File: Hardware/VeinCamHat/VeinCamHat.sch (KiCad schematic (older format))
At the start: 65 parts, among them J1 USB_B_Micro, J2 Raspberry_Pi_2_3, Q1 BSD235N, Q2 MMUN2133L, SW1 SW_SPST, U1 MCP3021, U2 TPS61092, U3 MCP73871

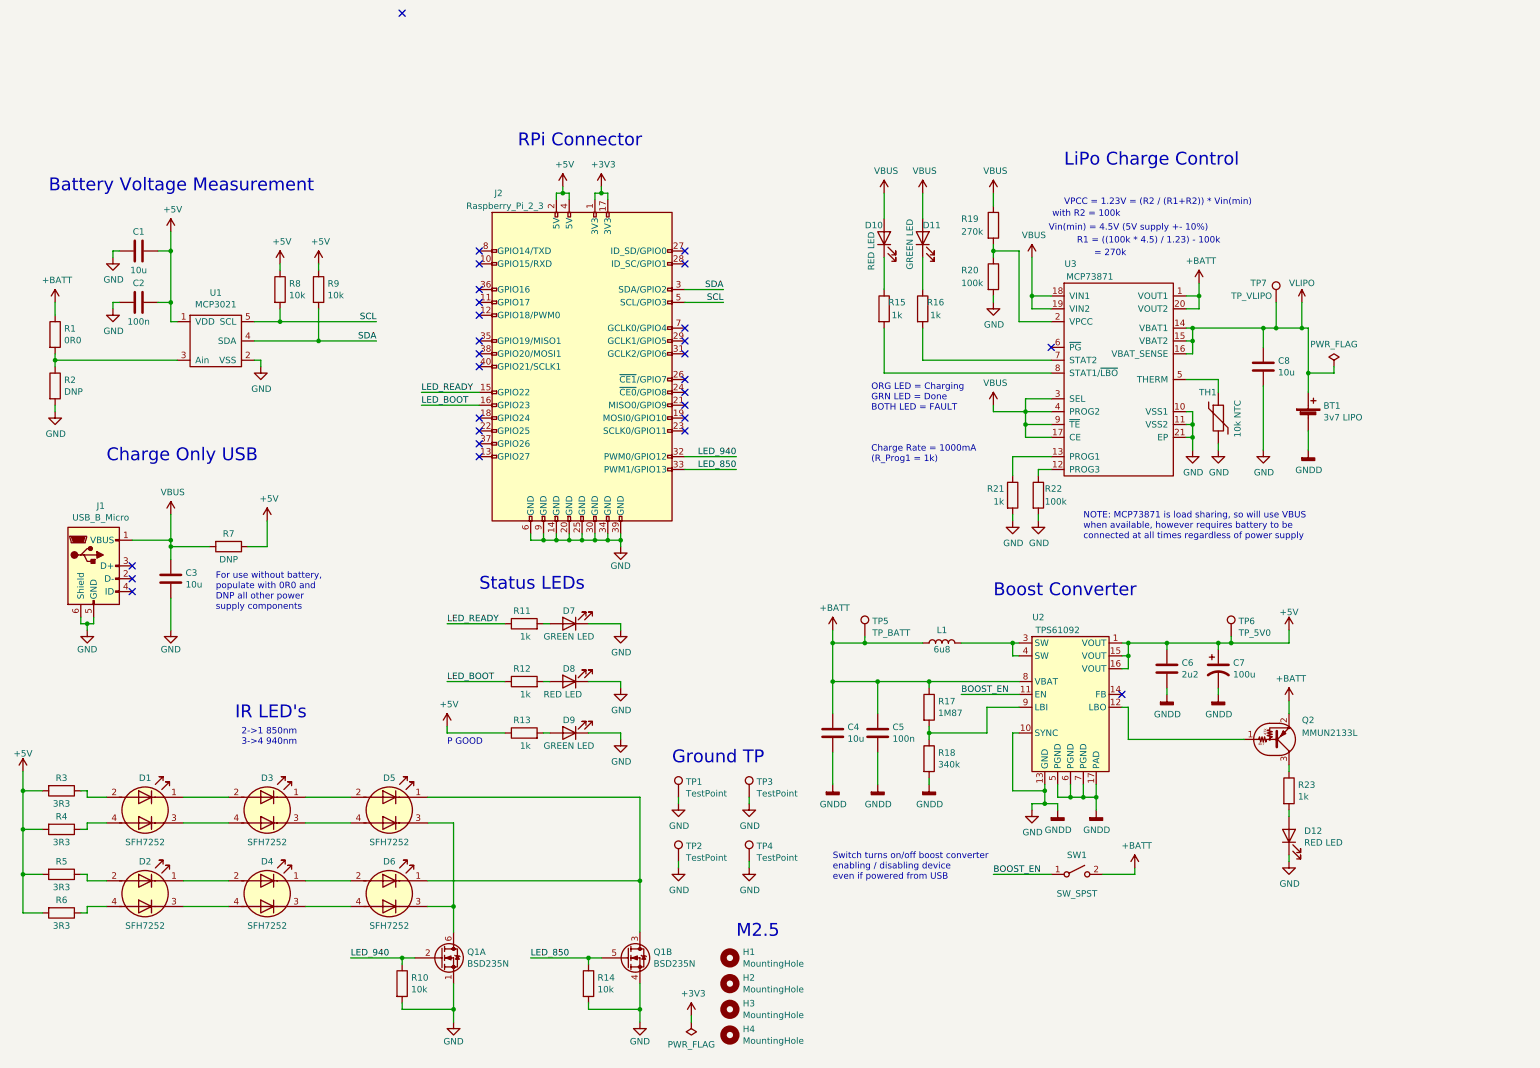
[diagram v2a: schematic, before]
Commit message: Added footprints for VeinCamHat and begun layout
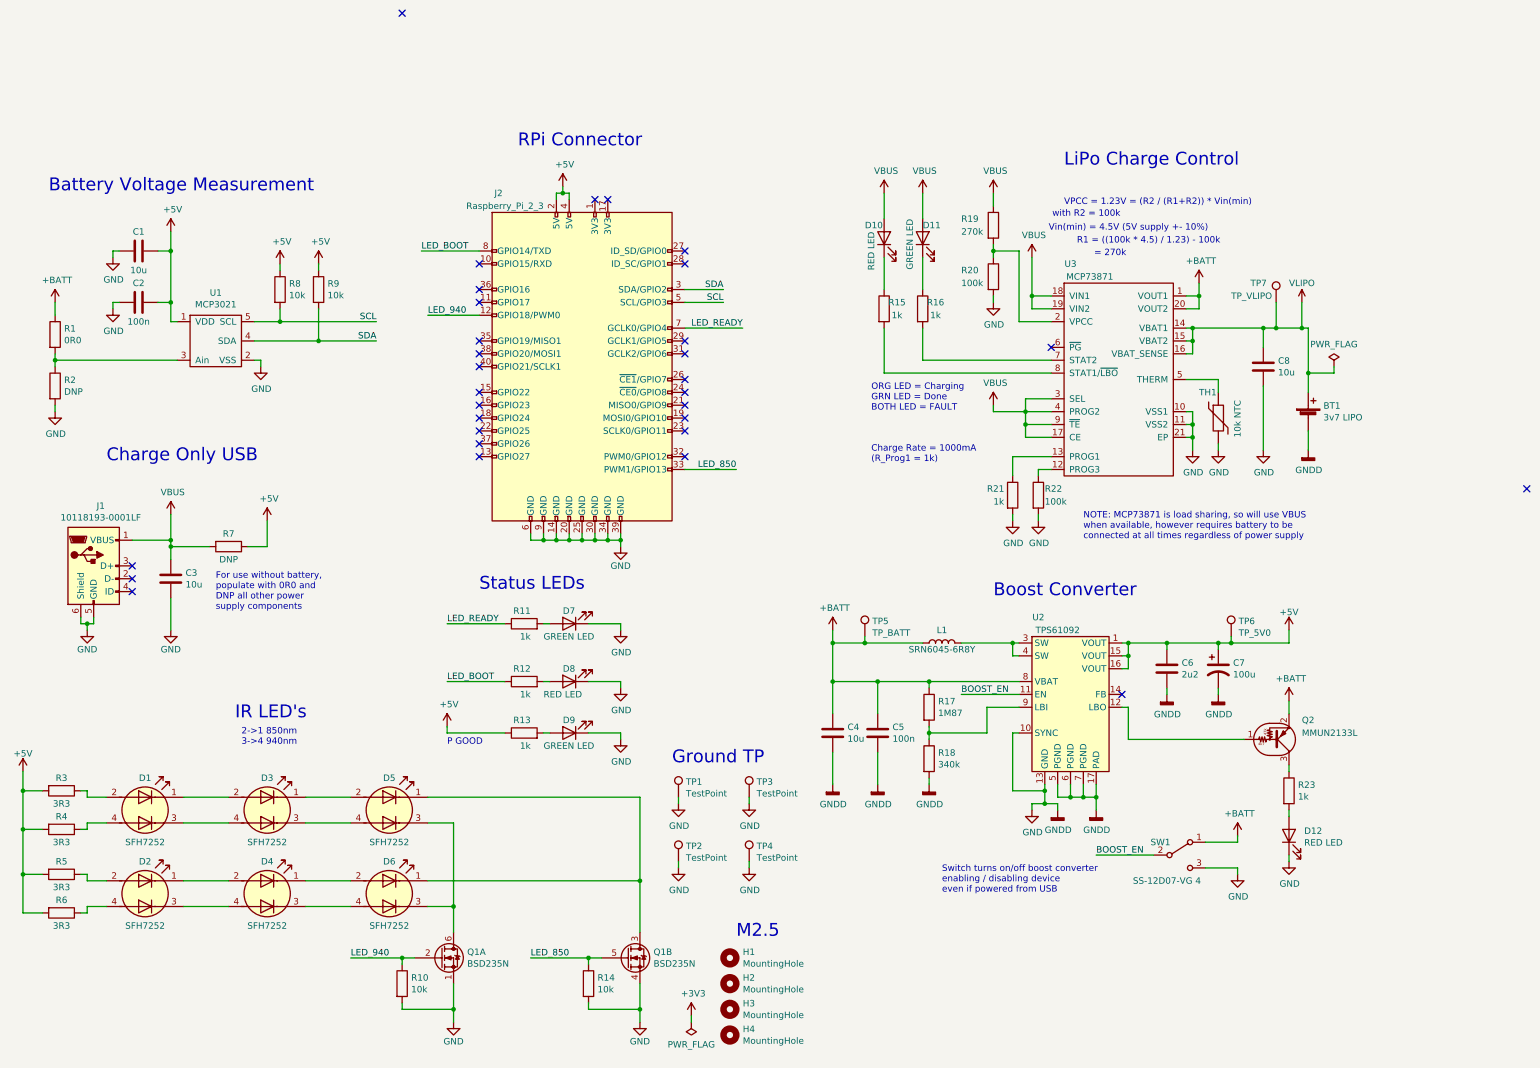
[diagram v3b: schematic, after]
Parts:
- removed SW1: SW_SPST, symbol Switch:SW_SPST
- added SW1: SS-12D07-VG 4, VeinCam_Footprints:SS-12D07-VG4, symbol Switch:SW_SPDT
- D1, D2, D3, D4, D5, D6: footprint (none) -> VeinCam_Footprints:SFH7252
- J1: value USB_B_Micro -> 10118193-0001LF; footprint (none) -> VeinCam_Footprints:10118193-0001LF
- J2: footprint (none) -> Connector_PinSocket_2.54mm:PinSocket_2x20_P2.54mm_Vertical
- L1: value 6u8 -> SRN6045-6R8Y; footprint (none) -> VeinCam_Footprints:SRN6045
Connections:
- net +3V3: no longer J2.1 (3V3), J2.17 (3V3)
- net +BATT: now also SW1.1 (A)
- net BOOST_EN: now also SW1.2 (B)
- net GND: now also SW1.3 (C)
- net LED_940: now also J2.12 (GPIO18/PWM0); no longer J2.32 (PWM0/GPIO12)
- net LED_BOOT: now also J2.8 (GPIO14/TXD); no longer J2.16 (GPIO23)
- net LED_READY: now also J2.7 (GCLK0/GPIO4); no longer J2.15 (GPIO22)
- no-connect marks 28 -> 31
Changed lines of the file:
@@
 P 1250 3900
 F 0 "J1" H 1305 4367 50  0000 C CNN
-F 1 "USB_B_Micro" H 1305 4276 50  0000 C CNN
-F 2 "" H 1400 3850 50  0001 C CNN
+F 1 "10118193-0001LF" H 1305 4276 50  0000 C CNN
+F 2 "VeinCam_Footprints:10118193-0001LF" H 1400 3850 50  0001 C CNN
 F 3 "~" H 1400 3850 50  0001 C CNN
 	1    1250 3900
@@
 P 7850 4500
 F 0 "L1" V 7950 4500 50  0000 C CNN
-F 1 "6u8" V 7800 4500 50  0000 C CNN
-F 2 "" H 7850 4500 50  0001 C CNN
+F 1 "SRN6045-6R8Y" V 7800 4500 50  0000 C CNN
+F 2 "VeinCam_Footprints:SRN6045" H 7850 4500 50  0001 C CNN
 F 3 "~" H 7850 4500 50  0001 C CNN
 	1    7850 4500
@@
 Wire Wire Line
 	7350 4800 7750 4800
-Text Label 8250 6300 0    50   ~ 0
+Text Label 9050 6150 0    50   ~ 0
 BOOST_EN
 Wire Wire Line
-	8250 6300 8700 6300
-$Comp
-L Switch:SW_SPST SW1
-U 1 1 5CF1111C
-P 8900 6300
-F 0 "SW1" H 8900 6450 50  0000 C CNN
-F 1 "SW_SPST" H 8900 6150 50  0000 C CNN
-F 2 "" H 8900 6300 50  0001 C CNN
-F 3 "" H 8900 6300 50  0001 C CNN
-	1    8900 6300
-	1    0    0    -1
-$EndComp
-Wire Wire Line
-	9100 6300 9350 6300
-Wire Wire Line
-	9350 6300 9350 6250
+	9050 6150 9500 6150
+Wire Wire Line
+	9900 6050 10150 6050
+Wire Wire Line
+	10150 6050 10150 6000
 $Comp
 L power:+BATT #PWR0130
 U 1 1 5CF1F81A
-P 9350 6250
-F 0 "#PWR0130" H 9350 6100 50  0001 C CNN
-F 1 "+BATT" H 9365 6423 50  0000 C CNN
-F 2 "" H 9350 6250 50  0001 C CNN
-F 3 "" H 9350 6250 50  0001 C CNN
-	1    9350 6250
-	1    0    0    -1
-$EndComp
-Text Notes 7000 6350 0    50   ~ 0
+P 10150 6000
+F 0 "#PWR0130" H 10150 5850 50  0001 C CNN
+F 1 "+BATT" H 10165 6173 50  0000 C CNN
+F 2 "" H 10150 6000 50  0001 C CNN
+F 3 "" H 10150 6000 50  0001 C CNN
+	1    10150 6000
+	1    0    0    -1
+$EndComp
+Text Notes 7850 6450 0    50   ~ 0
 Switch turns on/off boost converter\nenabling / disabling device\neven if powered from USB
 Text Notes 8950 3700 0    50   ~ 0
@@
 F 0 "J2" H 4400 3700 50  0000 C CNN
 F 1 "Raspberry_Pi_2_3" H 4450 3600 50  0000 C CNN
-F 2 "" H 5050 2350 50  0001 C CNN
+F 2 "Connector_PinSocket_2.54mm:PinSocket_2x20_P2.54mm_Vertical" H 5050 2350 50  0001 C CNN
 F 3 "https://www.raspberrypi.org/documentation/hardware/raspberrypi/schematics/rpi_SCH_3bplus_1p0_reduced.pdf" H 5050 2350 50  0001 C CNN
 	1    5050 2350
@@
 	1    0    0    -1
 $EndComp
-$Comp
-L power:+3V3 #PWR0137
-U 1 1 5D44522B
-P 5200 950
-F 0 "#PWR0137" H 5200 800 50  0001 C CNN
-F 1 "+3V3" H 5215 1123 50  0000 C CNN
-F 2 "" H 5200 950 50  0001 C CNN
-F 3 "" H 5200 950 50  0001 C CNN
-	1    5200 950
-	1    0    0    -1
-$EndComp
 NoConn ~ 5850 1450
 NoConn ~ 5850 1550
 Wire Wire Line
-	5850 3050 6250 3050
+	4250 1950 3850 1950
 Wire Wire Line
 	5850 3150 6250 3150
-Text Label 6250 3050 2    50   ~ 0
+Text Label 3850 1950 0    50   ~ 0
 LED_940
 Text Label 6250 3150 2    50   ~ 0
@@
 	5500 6350 5500 6750
 Connection ~ 5500 6350
-Text Label 3800 2550 0    50   ~ 0
+Text Label 6300 2050 2    50   ~ 0
 LED_READY
 Wire Wire Line
-	3800 2550 4250 2550
-Wire Wire Line
-	3800 2650 4250 2650
-Text Label 3800 2650 0    50   ~ 0
+	6300 2050 5850 2050
+Wire Wire Line
+	3800 1450 4250 1450
+Text Label 3800 1450 0    50   ~ 0
 LED_BOOT
 Text Label 4000 4350 0    50   ~ 0
@@
 F 0 "D1" H 1650 6050 50  0000 C CNN
 F 1 "SFH7252" H 1650 5550 50  0000 C CNN
-F 2 "" H 1680 5800 50  0001 C CNN
+F 2 "VeinCam_Footprints:SFH7252" H 1680 5800 50  0001 C CNN
 F 3 "~" H 1680 5800 50  0001 C CNN
 	1    1650 5800
@@
 F 0 "D2" H 1650 6700 50  0000 C CNN
 F 1 "SFH7252" H 1650 6200 50  0000 C CNN
-F 2 "" H 1680 6450 50  0001 C CNN
+F 2 "VeinCam_Footprints:SFH7252" H 1680 6450 50  0001 C CNN
 F 3 "~" H 1680 6450 50  0001 C CNN
 	1    1650 6450
@@
 F 0 "D4" H 2600 6700 50  0000 C CNN
 F 1 "SFH7252" H 2600 6200 50  0000 C CNN
-F 2 "" H 2630 6450 50  0001 C CNN
+F 2 "VeinCam_Footprints:SFH7252" H 2630 6450 50  0001 C CNN
 F 3 "~" H 2630 6450 50  0001 C CNN
 	1    2600 6450
@@
 F 0 "D6" H 3550 6700 50  0000 C CNN
 F 1 "SFH7252" H 3550 6200 50  0000 C CNN
-F 2 "" H 3580 6450 50  0001 C CNN
+F 2 "VeinCam_Footprints:SFH7252" H 3580 6450 50  0001 C CNN
 F 3 "~" H 3580 6450 50  0001 C CNN
 	1    3550 6450
@@
 F 0 "D5" H 3550 6050 50  0000 C CNN
 F 1 "SFH7252" H 3550 5550 50  0000 C CNN
-F 2 "" H 3580 5800 50  0001 C CNN
+F 2 "VeinCam_Footprints:SFH7252" H 3580 5800 50  0001 C CNN
 F 3 "~" H 3580 5800 50  0001 C CNN
 	1    3550 5800
@@
 F 0 "D3" H 2600 6050 50  0000 C CNN
 F 1 "SFH7252" H 2600 5550 50  0000 C CNN
-F 2 "" H 2630 5800 50  0001 C CNN
+F 2 "VeinCam_Footprints:SFH7252" H 2630 5800 50  0001 C CNN
 F 3 "~" H 2630 5800 50  0001 C CNN
 	1    2600 5800
@@
 	1    0    0    -1
 $EndComp
-NoConn ~ 4250 1450
 NoConn ~ 4250 1550
 NoConn ~ 4250 1750
 NoConn ~ 4250 1850
-NoConn ~ 4250 1950
 NoConn ~ 4250 2150
 NoConn ~ 4250 2250
@@
 NoConn ~ 5850 2250
 NoConn ~ 5850 2150
-NoConn ~ 5850 2050
-Wire Wire Line
-	5150 1050 5150 1000
-Wire Wire Line
-	5150 1000 5200 1000
-Wire Wire Line
-	5250 1000 5250 1050
-Wire Wire Line
-	5200 1000 5200 950
-Connection ~ 5200 1000
-Wire Wire Line
-	5200 1000 5250 1000
 $Comp
 L power:PWR_FLAG #FLG0101
@@
 	1    0    0    -1
 $EndComp
+$Comp
+L Switch:SW_SPDT SW1
+U 1 1 5C908079
+P 9700 6150
+F 0 "SW1" H 9550 6250 50  0000 C CNN
+F 1 "SS-12D07-VG 4" H 9600 5950 50  0000 C CNN
+F 2 "VeinCam_Footprints:SS-12D07-VG4" H 9700 6150 50  0001 C CNN
+F 3 "" H 9700 6150 50  0001 C CNN
+	1    9700 6150
+	1    0    0    -1
+$EndComp
+Wire Wire Line
+	9900 6250 10150 6250
+Wire Wire Line
+	10150 6250 10150 6300
+$Comp
+L power:GND #PWR0137
+U 1 1 5C942C6D
+P 10150 6300
+F 0 "#PWR0137" H 10150 6050 50  0001 C CNN
+F 1 "GND" H 10155 6127 50  0000 C CNN
+F 2 "" H 10150 6300 50  0001 C CNN
+F 3 "" H 10150 6300 50  0001 C CNN
+	1    10150 6300
+	1    0    0    -1
+$EndComp
+NoConn ~ 4250 2650
+NoConn ~ 5850 3050
+NoConn ~ 5150 1050
+NoConn ~ 5250 1050
+NoConn ~ 12400 3300
+NoConn ~ 4250 2550
 $EndSCHEMATC

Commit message: Changed plans for VeinCam Plus, both boards laid out
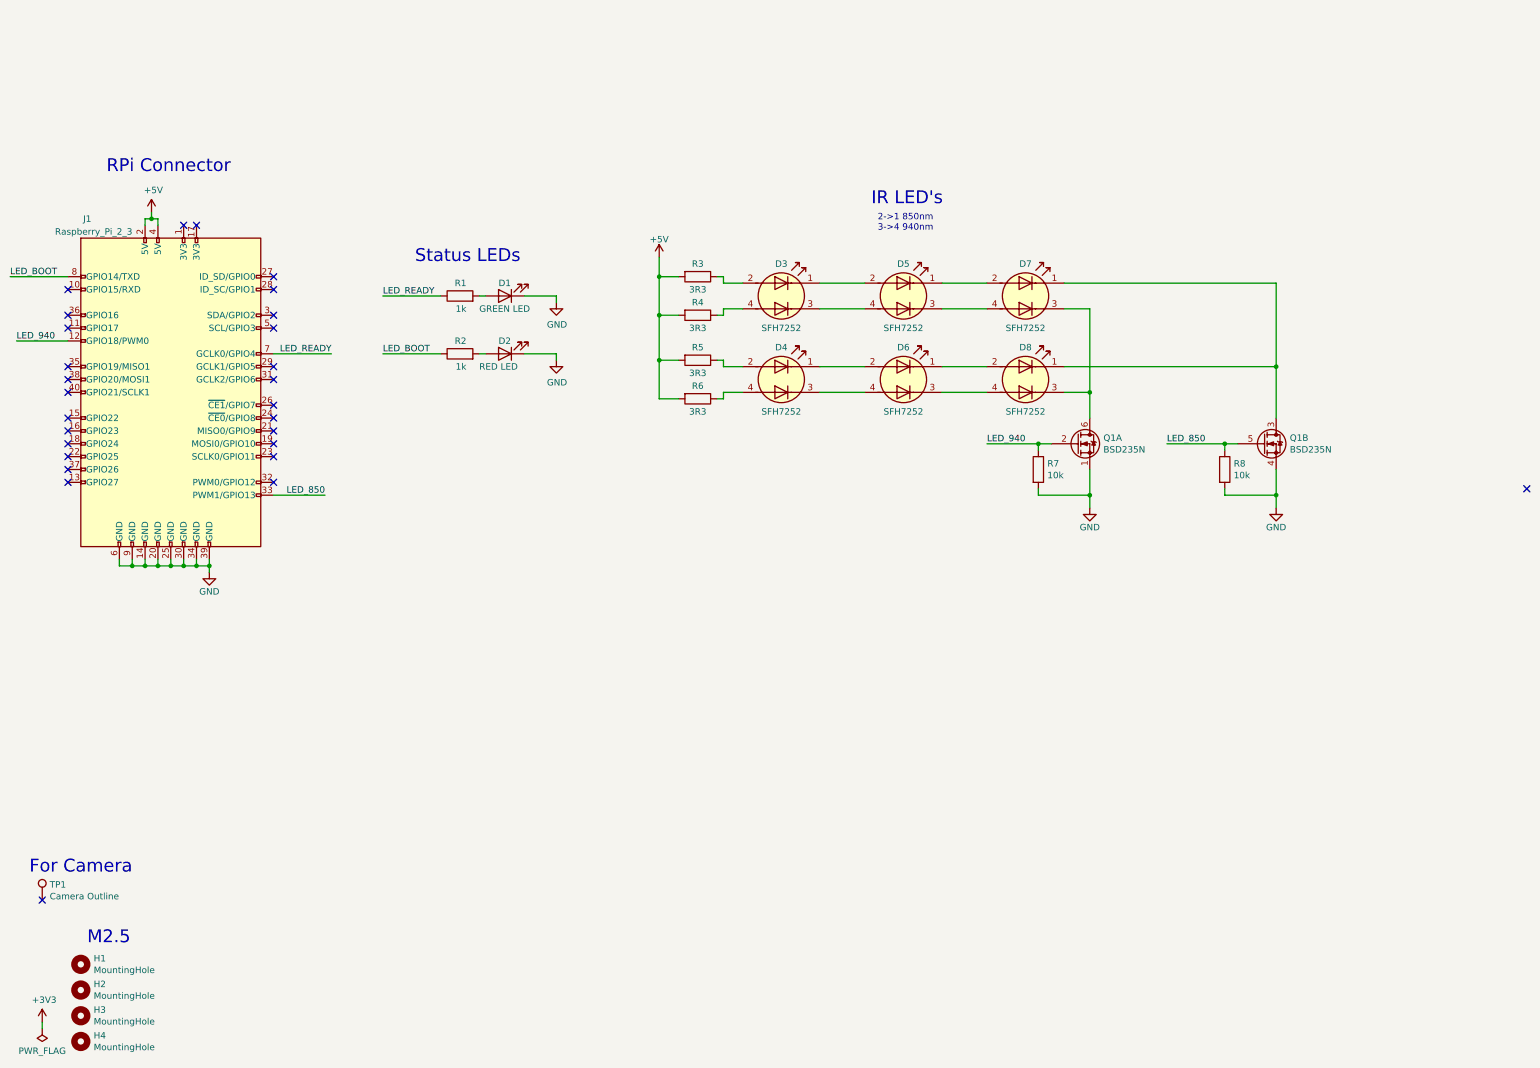
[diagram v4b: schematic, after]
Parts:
- removed BT1: 3v7 LIPO, Connector_JST:JST_XH_S02B-XH-A_1x02_P2.50mm_Horizontal, symbol Device:Battery_Cell
- removed C1, C3, C4, C8: 10u, Capacitor_SMD:C_0603_1608Metric, symbol Device:C
- removed C2, C5: 100n, Capacitor_SMD:C_0603_1608Metric, symbol Device:C
- removed C6: 2u2, Capacitor_SMD:C_0603_1608Metric, symbol Device:C
- removed C7: 100u, Capacitor_Tantalum_SMD:CP_EIA-7343-31_Kemet-D, symbol Device:CP1
- removed D10, D12: RED LED, LED_SMD:LED_0805_2012Metric, symbol Device:LED
- removed D11, D9: GREEN LED, LED_SMD:LED_0805_2012Metric, symbol Device:LED
- removed J1: 10118193-0001LF, VeinCam_Footprints:10118193-0001LF, symbol Connector:USB_B_Micro
- removed L1: SRN6045-6R8Y, VeinCam_Footprints:SRN6045, symbol Device:L
- removed Q2: MMUN2133L, Package_TO_SOT_SMD:SOT-23, symbol Transistor_BJT:DTA143Z
- removed R1: 0R0, Resistor_SMD:R_0603_1608Metric, symbol Device:R
- removed R13, R15, R16, R21, R23: 1k, Resistor_SMD:R_0603_1608Metric, symbol Device:R
- removed R17: 1M87, Resistor_SMD:R_0603_1608Metric, symbol Device:R
- removed R18: 340k, Resistor_SMD:R_0603_1608Metric, symbol Device:R
- removed R19: 270k, Resistor_SMD:R_0603_1608Metric, symbol Device:R
- removed R2: DNP, Resistor_SMD:R_0603_1608Metric, symbol Device:R
- removed R20, R22: 100k, Resistor_SMD:R_0603_1608Metric, symbol Device:R
- removed R7: DNP, Resistor_SMD:R_1206_3216Metric, symbol Device:R
- removed R8, R9: 10k, Resistor_SMD:R_0603_1608Metric, symbol Device:R
- removed SW1: SS-12D07-VG 4, VeinCam_Footprints:SS-12D07-VG4, symbol Switch:SW_SPDT
- removed TH1: 10k NTC, Resistor_SMD:R_0603_1608Metric, symbol Device:Thermistor
- removed TP2, TP3, TP4: TestPoint, TestPoint:TestPoint_THTPad_D1.0mm_Drill0.5mm, symbol Connector:TestPoint
- removed TP5: TP_BATT, TestPoint:TestPoint_Pad_D1.0mm, symbol Connector:TestPoint
- removed TP6: TP_5V0, TestPoint:TestPoint_Pad_D1.0mm, symbol Connector:TestPoint
- removed TP7: TP_VLIPO, TestPoint:TestPoint_Pad_D1.0mm, symbol Connector:TestPoint
- removed U1: MCP3021, Package_TO_SOT_SMD:SOT-23-5, symbol VeinCam_Symbols:MCP3021
- removed U2: TPS61092, Package_DFN_QFN:QFN-16-1EP_4x4mm_P0.65mm_EP2.5x2.5mm, symbol Regulator_Switching:TPS61092
- removed U3: MCP73871, Package_DFN_QFN:QFN-20-1EP_4x4mm_P0.5mm_EP2.5x2.5mm, symbol VeinCam_Symbols:MCP73871
- TP1: value TestPoint -> Camera Outline; footprint TestPoint:TestPoint_THTPad_D1.0mm_Drill0.5mm -> VeinCam_Footprints:PiCamera
- renumbered D7 to D1, D8 to D2, D1 to D3, D2 to D4, D3 to D5, D4 to D6, D5 to D7, D6 to D8, J2 to J1, R11 to R1, R12 to R2, R10 to R7, R14 to R8
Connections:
- net GND: no longer TP1.1
- net SCL: no longer names the net of J1.5 (SCL/GPIO3)
- net SDA: no longer names the net of J1.3 (SDA/GPIO2)
- no-connect marks 31 -> 28
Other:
- note added: "For Camera"
- note removed: "= 270k"
- note removed: "Battery Voltage Measurement"
- note removed: "Boost Converter"
- note removed: "Charge Only USB\n"
- note removed: "Charge Rate = 1000mA\n(R_Prog1 = 1k)\n"
- note removed: "For use without battery, \npopulate with 0R0 and\nDNP all other power \nsupply components"
- note removed: "Ground TP"
- note removed: "LiPo Charge Control\n"
- note removed: "NOTE: MCP73871 is load sharing, so will use VBUS\nwhen available, however requires battery to be \nconnected at all times regardless of power supply"
- note removed: "ORG LED = Charging\nGRN LED = Done\nBOTH LED = FAULT"
- note removed: "P GOOD"
- note removed: "R1 = ((100k * 4.5) / 1.23) - 100k\n"
- note removed: "Switch turns on/off boost converter\nenabling / disabling device\neven if powered from USB"
- note removed: "VPCC = 1.23V = (R2 / (R1+R2)) * Vin(min)"
- note removed: "Vin(min) = 4.5V (5V supply +- 10%)\n"
- note removed: "with R2 = 100k"
- moved on the sheet: D1, D2, D3, D4, D5, D6, D7, D8, H1, H2, H3, H4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

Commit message: More Hardware changes, both boards complete
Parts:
- removed Q1: BSD235N, Package_TO_SOT_SMD:SOT-363_SC-70-6, symbol VeinCam_Symbols:BSD235N
- added Q1: NTJD4001N, Package_TO_SOT_SMD:SOT-363_SC-70-6, symbol VeinCam_Symbols:NTJD4001N
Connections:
- net GND: now also Q1.1 (S), Q1.4 (S)
- net LED_850: now also Q1.5 (G)
- net LED_940: now also Q1.2 (G)
- net at D7.3 (K1), D8.3 (K1): now also Q1.6 (D)
- net at D7.1 (K2), D8.1 (K2): now also Q1.3 (D)
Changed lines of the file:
@@
 	4600 2250 4850 2250
-$Comp
-L VeinCam_Symbols:BSD235N Q1
-U 1 1 5C89B330
-P 8900 2950
-F 0 "Q1" H 9106 2996 50  0000 L CNN
-F 1 "BSD235N" H 9106 2905 50  0000 L CNN
-F 2 "Package_TO_SOT_SMD:SOT-363_SC-70-6" H 9100 2950 50  0001 C CNN
-F 3 "~" H 9100 2950 50  0001 C CNN
-	1    8900 2950
-	1    0    0    -1
-$EndComp
-$Comp
-L VeinCam_Symbols:BSD235N Q1
-U 2 1 5C89B4BB
-P 10350 2950
-F 0 "Q1" H 10556 2996 50  0000 L CNN
-F 1 "BSD235N" H 10556 2905 50  0000 L CNN
-F 2 "Package_TO_SOT_SMD:SOT-363_SC-70-6" H 10550 2950 50  0001 C CNN
-F 3 "~" H 10550 2950 50  0001 C CNN
-	2    10350 2950
-	1    0    0    -1
-$EndComp
 $Comp
 L VeinCam_Symbols:SFH7252 D3
@@
 NoConn ~ 2650 1950
 NoConn ~ 2650 2050
+$Comp
+L VeinCam_Symbols:NTJD4001N Q1
+U 1 1 5C91E58D
+P 8900 2950
+F 0 "Q1" H 9106 2996 50  0000 L CNN
+F 1 "NTJD4001N" H 9106 2905 50  0000 L CNN
+F 2 "Package_TO_SOT_SMD:SOT-363_SC-70-6" H 9100 2950 50  0001 C CNN
+F 3 "~" H 9100 2950 50  0001 C CNN
+	1    8900 2950
+	1    0    0    -1
+$EndComp
+$Comp
+L VeinCam_Symbols:NTJD4001N Q1
+U 2 1 5C91E612
+P 10350 2950
+F 0 "Q1" H 10556 2996 50  0000 L CNN
+F 1 "NTJD4001N" H 10556 2905 50  0000 L CNN
+F 2 "Package_TO_SOT_SMD:SOT-363_SC-70-6" H 10550 2950 50  0001 C CNN
+F 3 "~" H 10550 2950 50  0001 C CNN
+	2    10350 2950
+	1    0    0    -1
+$EndComp
 $EndSCHEMATC
